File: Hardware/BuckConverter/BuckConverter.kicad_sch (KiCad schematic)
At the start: 0 parts

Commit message: started buck converter schematic
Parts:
- added C1: C, symbol Device:C
- added C2: 100n, symbol Device:C
- added J2: Screw_Terminal_01x02, symbol Connector:Screw_Terminal_01x02
- added L1: L, symbol Device:L
- added Q1, Q2: DMT6012LSS, kicadLibFp:SO8-DiodeInc, symbol KicadLib:DMT6012LSS
- added R1, R2, R3: R, symbol Device:R
- added U1: LTC4444-5, symbol KicadLib:LTC4444-5
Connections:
- new net: C2.1, U1.6
- new net: C2.2, L1.1, Q1.1 (D), Q2.3 (S), U1.8 (TS)
- new net: L1.2, R1.1
- new net: R2.1, U1.4 (BG)
- new net: Q1.2 (G), R2.2
- new net: Q2.2 (G), R3.2
- new net: R3.1, U1.7 (TG)
- new net: C1.1, J2.1 (Pin_1), R1.2
- new net +5v: U1.3 (VCC)
- new net GND: C1.2, J2.2 (Pin_2), Q1.3 (S), U1.9
- new net Vbatt: Q2.1 (D)

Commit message: buck converter V1
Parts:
- removed U1: LTC4444-5, symbol KicadLib:LTC4444-5
- added C3: C, symbol Device:C
- added J3: Screw_Terminal_01x02, symbol Connector:Screw_Terminal_01x02
- added R4: R, symbol Device:R
- added R5: 60k, symbol Device:R
- added R6, R8: 20k, symbol Device:R
- added R7: 390k, symbol Device:R
- added R9: 62, symbol Device:R
- added U1: UCC27282, kicadLibFp:SOIC-8, symbol KicadLib:UCC27282
- added U2: STEF01, symbol KicadLib:STEF01
- added U4: INA296A2, symbol KicadLib:INA296A2
- C1: value C -> 220u
- L1: value L -> 100u
- R1: value R -> 30m
- R2, R3: value R -> 10
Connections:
- net GND: now also J3.1 (Pin_1), R6.1, R8.1, U1.7, U2.3, U4. (REF2)
- net Vbatt: now also R7.2; no longer Q2.1 (D)
- net at C2.1: now also U1.2
- net at C2.2, L1.1, Q1.1 (D)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: now also C3.2, U1.4 (HS)
- net at L1.2, R1.1: now also R4.2, U4. (REF2)
- net at R2.1: now also U1.8 (LO)
- net at R3.1: now also U1.3 (HO)
- net at C1.1, J2.1 (Pin_1), R1.2: now also R5.2, U4. (REF2)
- new net: R7.1, R8.2, U2.1 (UVLO)
- new net: R9.1, U2.10 (Ilim)
- new net: C3.1, R4.1
- new net: J3.2 (Pin_2), U2.14 (Vcc), U2.15
- new net +3v3: U4. (REF2)
- new net +8v: U1.1 (VDD)
- new net En/Fault: U2.12 (En/Fault)
- new net Isense: U4. (REF2)
- new net PG: U2.13 (PG)
- new net PWM-A: U1.5 (HI)
- new net PWM-B: U1.6 (LI)
- new net V_Sense: R5.1, R6.2
- new net Vin: Q2.1 (D), R9.2, U2.6 (Vout), U2.7 (Vout), U2.8 (Vout), U2.9 (Vout)
- no-connect marks 0 -> 4
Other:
- moved on the sheet: C1, C2, J2, L1, Q1, Q2, R1, R2, R3

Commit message: Schematic V2 added board comunication connectors and decoupling C
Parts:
- added C4, C6, C9: 100n, symbol Device:C
- added C5: 100u, symbol Device:C
- added C7: 4u7, symbol Device:C
- added C8: 1u, symbol Device:C
- added J1: PWR Conn, symbol Connector_Generic:Conn_02x04_Top_Bottom
- added J4: Conn_02x07_Top_Bottom, symbol Connector_Generic:Conn_02x07_Top_Bottom
- added J6: Ana Conn, symbol Connector_Generic:Conn_02x05_Top_Bottom
- added R10, R11: 100k, symbol Device:R
- C3, R4: now not fitted
- R5: value 60k -> 100k
- R9: value 62 -> 56
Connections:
- net +3v3: now also C6.2, J1.4 (Pin_4)
- net +8v: now also C4.2, C7.2, J1.3 (Pin_3)
- net En/Fault: now also J4.6 (Pin_6)
- net GND: now also C4.1, C5.1, C6.1, C7.1, C8.1, C9.1, J1.5 (Pin_5), J1.6 (Pin_6), J1.7 (Pin_7), J1.8 (Pin_8), J4.11 (Pin_11), J4.14 (Pin_14), J4.4 (Pin_4), J4.7 (Pin_7), J6.10 (Pin_10), J6.6 (Pin_6), J6.7 (Pin_7), J6.8 (Pin_8), J6.9 (Pin_9), R10.1, R11.1
- net Isense: now also J6.1 (Pin_1)
- net PG: now also J4.5 (Pin_5)
- net PWM-A: now also J4.1 (Pin_1)
- net PWM-B: now also J4.8 (Pin_8)
- net V_Sense: now also J6.4 (Pin_4)
- net Vin: now also C5.2, C8.2, C9.2, J1.1 (Pin_1), J1.2 (Pin_2)
- net at Q1.2 (G), R2.2: now also R11.2
- net at Q2.2 (G), R3.2: now also R10.2
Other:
- moved on the sheet: C1, C2, J2, L1, Q1, Q2, R1, R2, R3, R5, R6, U1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

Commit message: changed MOS driver capacity
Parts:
- C7: value 4u7 -> 10u
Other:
- moved on the sheet: C1, C6, J2, J3, R5, R6, R7, R8, U4

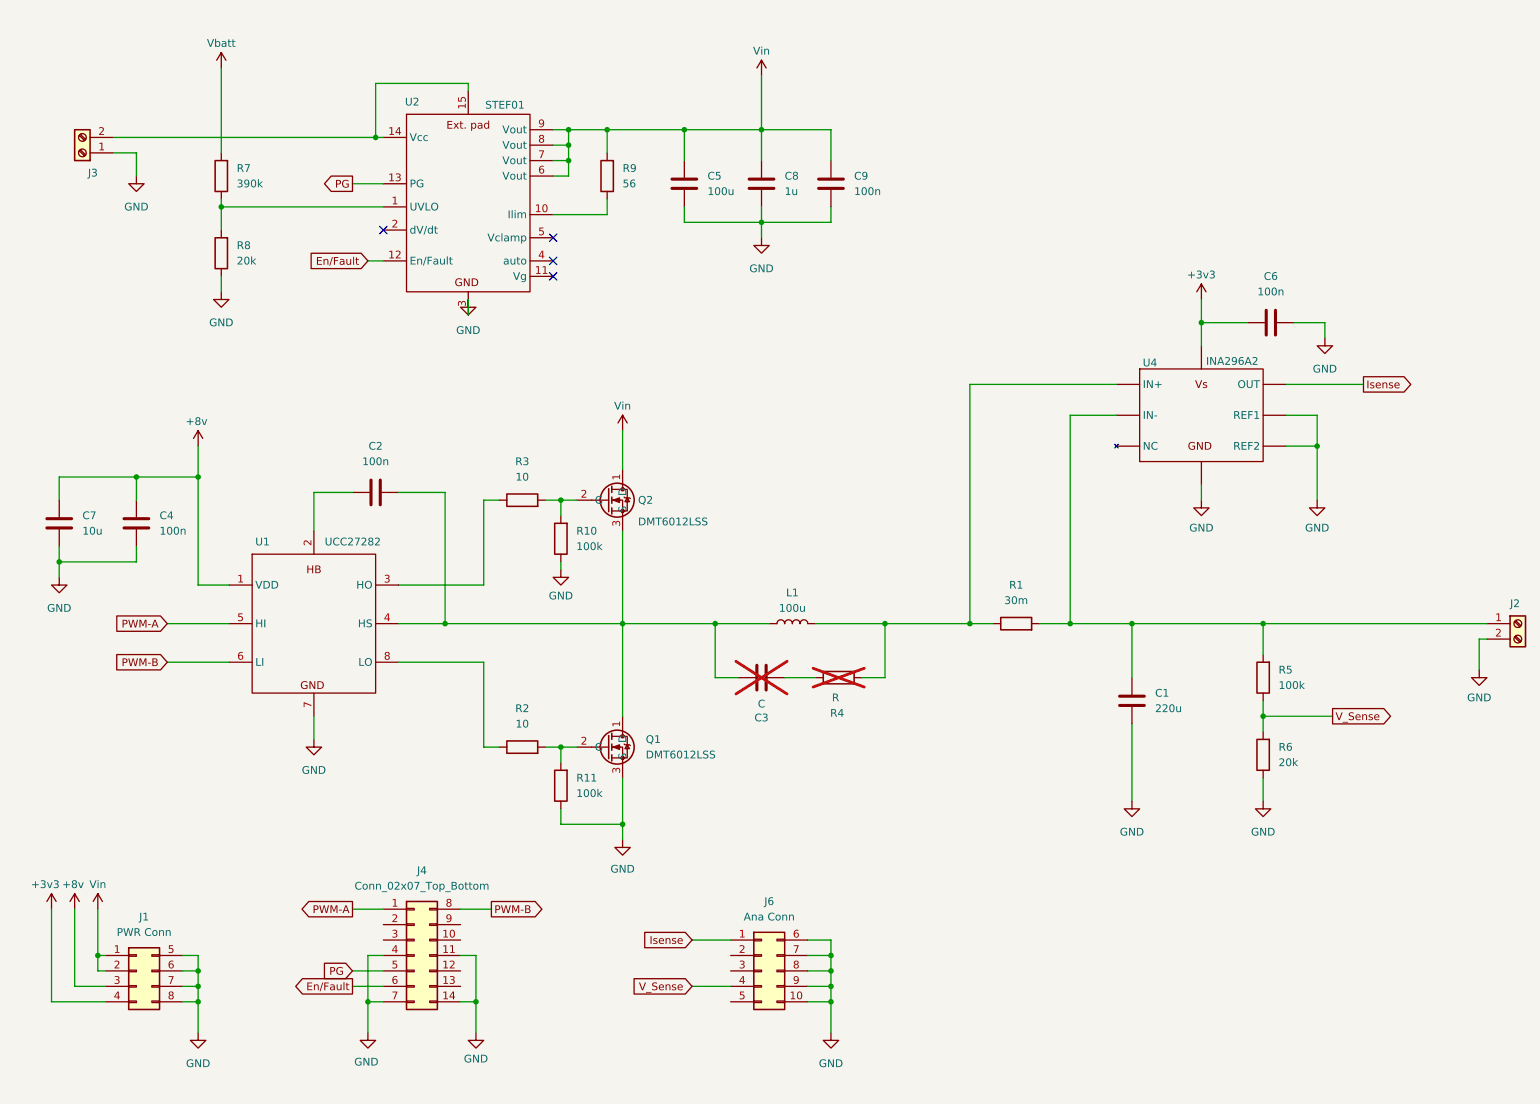
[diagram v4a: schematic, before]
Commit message: change connector size and gate voltage to 9V
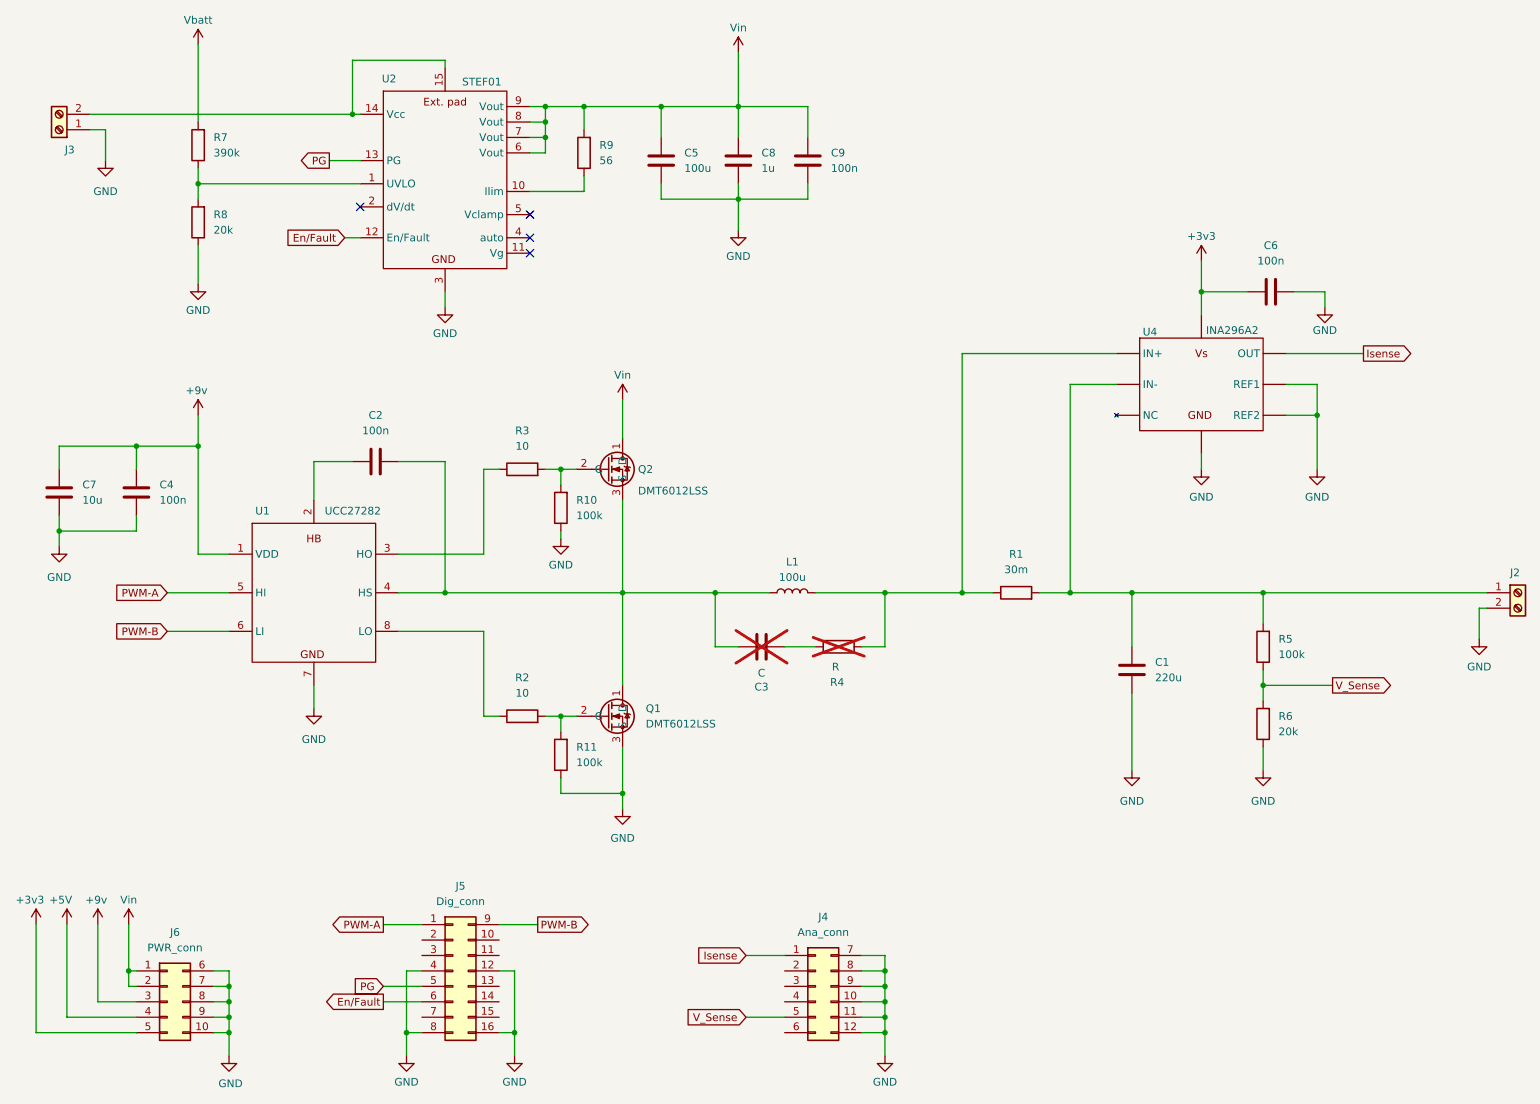
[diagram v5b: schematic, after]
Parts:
- removed J1: PWR Conn, symbol Connector_Generic:Conn_02x04_Top_Bottom
- removed J4: Conn_02x07_Top_Bottom, symbol Connector_Generic:Conn_02x07_Top_Bottom
- added J4: Ana_conn, symbol Connector_Generic:Conn_02x06_Top_Bottom
- added J5: Dig_conn, symbol Connector_Generic:Conn_02x08_Top_Bottom
- J6: value Ana Conn -> PWR_conn
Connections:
- net +8v is gone; now on net +9v: C4.2, C7.2, U1.1 (VDD)
- net +3v3: now also J6.5 (Pin_5)
- net En/Fault: now also J5.6 (Pin_6)
- net GND: now also J4.10 (Pin_10), J4.11 (Pin_11), J4.12 (Pin_12), J4.7 (Pin_7), J4.8 (Pin_8), J4.9 (Pin_9), J5.12 (Pin_12), J5.16 (Pin_16), J5.4 (Pin_4), J5.8 (Pin_8)
- net Isense: now also J4.1 (Pin_1); no longer J6.1 (Pin_1)
- net PG: now also J5.5 (Pin_5)
- net PWM-A: now also J5.1 (Pin_1)
- net PWM-B: now also J5.9 (Pin_9)
- net V_Sense: now also J4.5 (Pin_5); no longer J6.4 (Pin_4)
- net Vin: now also J6.1 (Pin_1), J6.2 (Pin_2)
- net +9v: now reaches J6.3 (Pin_3)
- new net +5V: J6.4 (Pin_4)
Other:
- moved on the sheet: C1, C2, C3, C4, C5, C6, C7, C8, C9, J2, J3, L1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
